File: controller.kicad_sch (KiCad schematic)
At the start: 3 parts

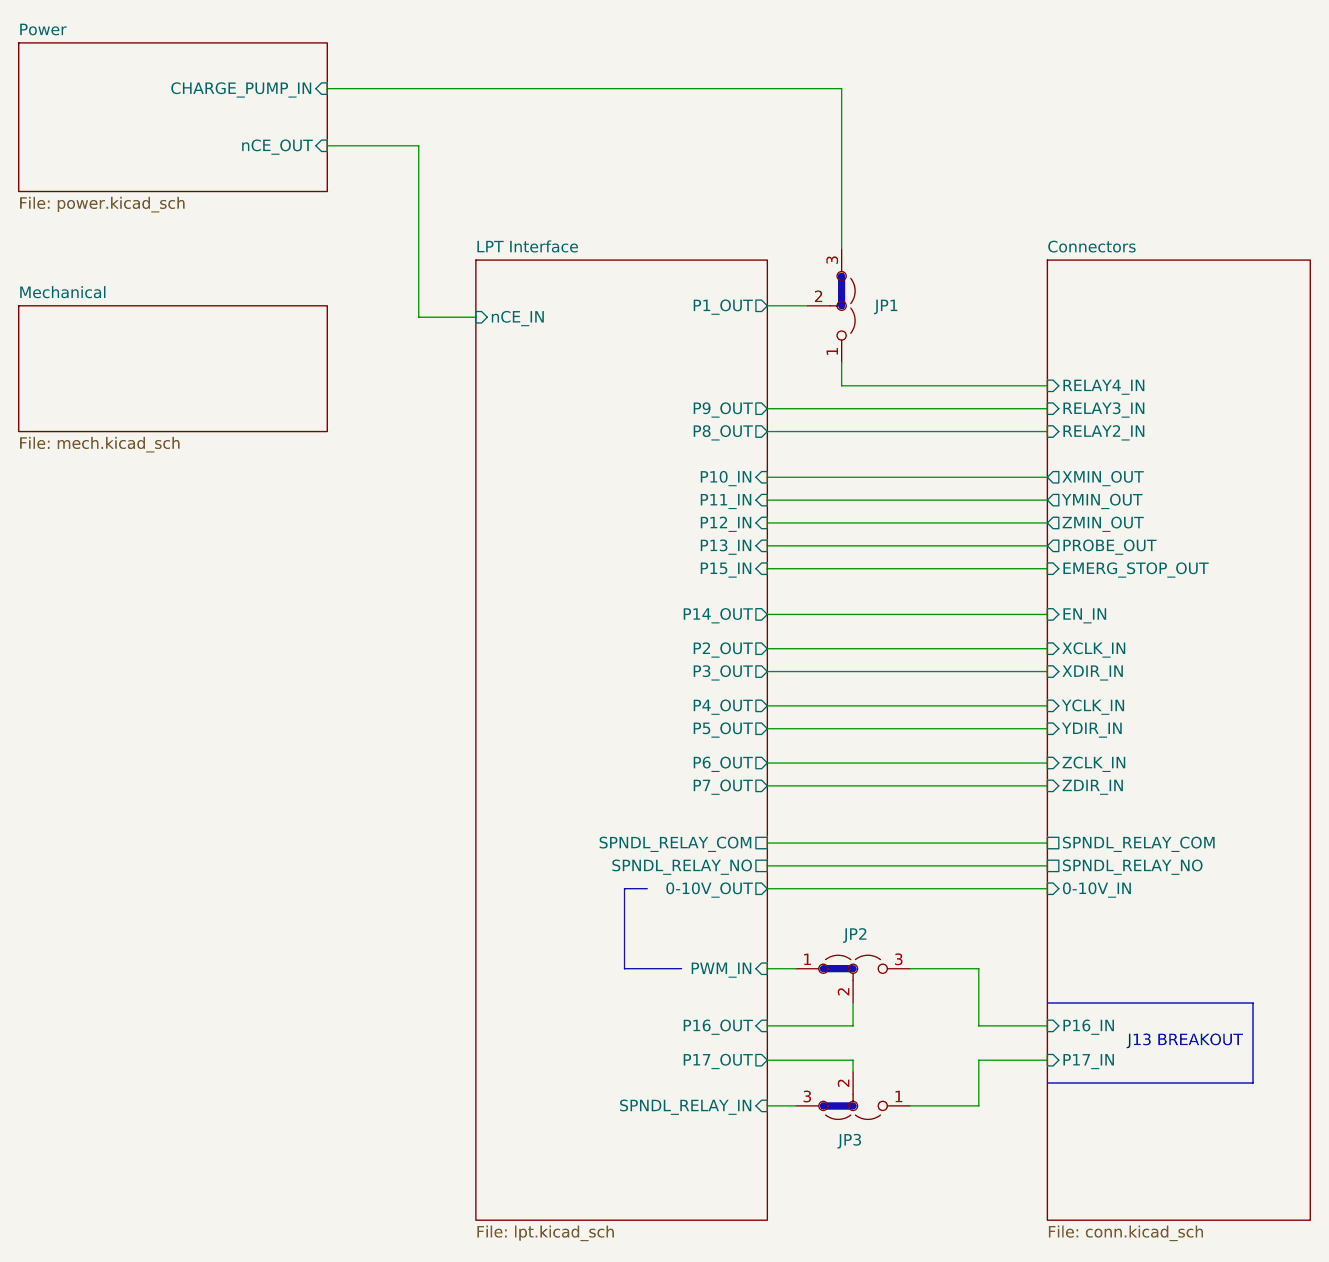
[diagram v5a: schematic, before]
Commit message: DRC checks. Tagging as V1.0 'actual'
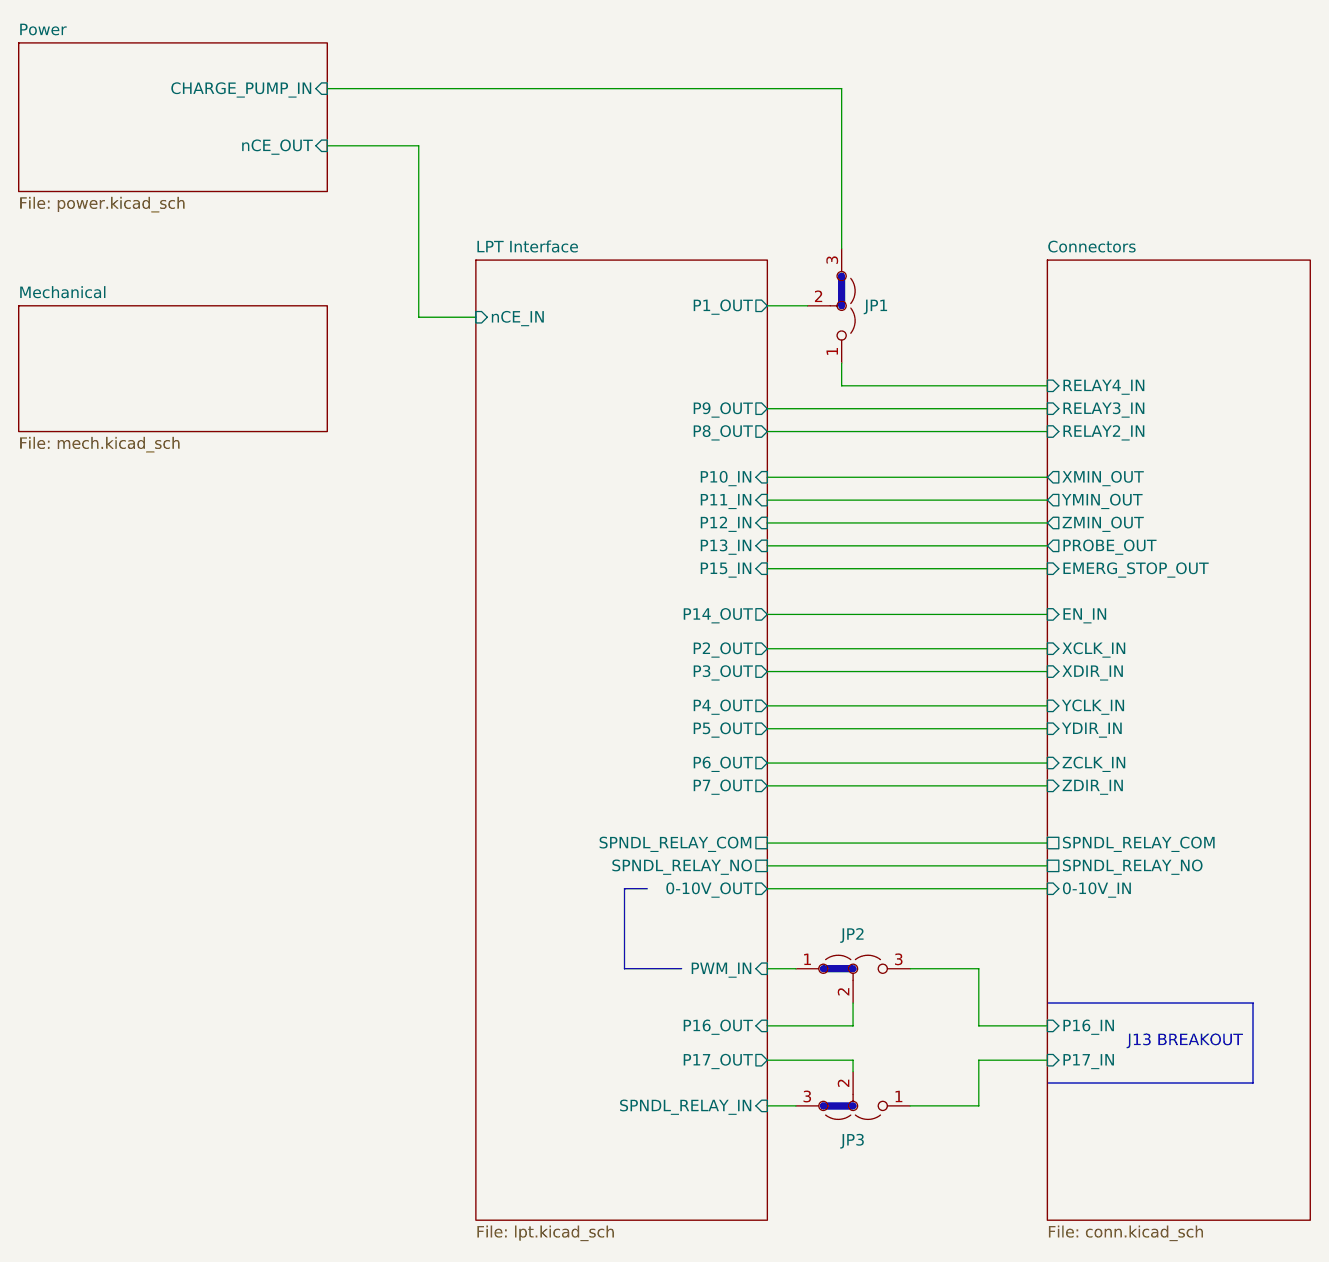
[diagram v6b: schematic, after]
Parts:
- JP1, JP2, JP3: value 1x02_2.54 -> (none); footprint Connector_PinHeader_2.54mm:PinHeader_1x03_P2.54mm_Vertical -> (none); E14MOQ 50 -> (none); E14PART 1593411 -> (none); JLCMFR# DNI -> (none)
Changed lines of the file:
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@@
+    (stroke (width 0) (type default) (color 0 0 0 0))
+  )
+  (wire (pts (xy 154.305 120.65) (xy 185.42 120.65))
+    (stroke (width 0) (type default) (color 0 0 0 0))
+  )
+  (wire (pts (xy 177.8 147.32) (xy 177.8 142.24))
+    (stroke (width 0) (type default) (color 0 0 0 0))
+  )
+  (polyline (pts (xy 185.42 144.78) (xy 208.28 144.78))
+    (stroke (width 0) (type default) (color 0 0 0 0))
+  )
+  (wire (pts (xy 115.57 59.69) (xy 121.92 59.69))
+    (stroke (width 0) (type default) (color 0 0 0 0))
+  )
+  (wire (pts (xy 154.305 77.47) (xy 185.42 77.47))
+    (stroke (width 0) (type default) (color 0 0 0 0))
+  )
+  (wire (pts (xy 177.8 132.08) (xy 177.8 138.43))
+    (stroke (width 0) (type default) (color 0 0 0 0))
+  )
+  (wire (pts (xy 154.305 132.08) (xy 157.48 132.08))
+    (stroke (width 0) (type default) (color 0 0 0 0))
+  )
+  (wire (pts (xy 162.56 34.29) (xy 105.41 34.29))
+    (stroke (width 0) (type default) (color 0 0 0 0))
+  )
+  (wire (pts (xy 154.305 80.01) (xy 185.42 80.01))
+    (stroke (width 0) (type default) (color 0 0 0 0))
+  )
+  (wire (pts (xy 154.305 58.42) (xy 158.75 58.42))
+    (stroke (width 0) (type default) (color 0 0 0 0))
+  )
+  (polyline (pts (xy 138.43 132.08) (xy 138.43 123.19))
     (stroke (width 0) (type default) (color 0 0 0 0))
   )
   (wire (pts (xy 163.83 142.24) (xy 163.83 143.51))
-    (stroke (width 0) (type default) (color 0 0 0 0))
-  )
-  (wire (pts (xy 154.305 120.65) (xy 185.42 120.65))
-    (stroke (width 0) (type default) (color 0 0 0 0))
-  )
-  (wire (pts (xy 177.8 147.32) (xy 177.8 142.24))
-    (stroke (width 0) (type default) (color 0 0 0 0))
-  )
-  (polyline (pts (xy 185.42 144.78) (xy 208.28 144.78))
-    (stroke (width 0) (type default) (color 0 0 0 0))
-  )
-  (wire (pts (xy 115.57 59.69) (xy 121.92 59.69))
-    (stroke (width 0) (type default) (color 0 0 0 0))
-  )
-  (wire (pts (xy 154.305 77.47) (xy 185.42 77.47))
-    (stroke (width 0) (type default) (color 0 0 0 0))
-  )
-  (wire (pts (xy 177.8 132.08) (xy 177.8 138.43))
-    (stroke (width 0) (type default) (color 0 0 0 0))
-  )
-  (wire (pts (xy 154.305 132.08) (xy 157.48 132.08))
-    (stroke (width 0) (type default) (color 0 0 0 0))
-  )
-  (wire (pts (xy 162.56 34.29) (xy 105.41 34.29))
-    (stroke (width 0) (type default) (color 0 0 0 0))
-  )
-  (wire (pts (xy 154.305 80.01) (xy 185.42 80.01))
-    (stroke (width 0) (type default) (color 0 0 0 0))
-  )
-  (wire (pts (xy 154.305 58.42) (xy 158.75 58.42))
-    (stroke (width 0) (type default) (color 0 0 0 0))
-  )
-  (polyline (pts (xy 138.43 132.08) (xy 138.43 123.19))
     (stroke (width 0) (type default) (color 0 0 0 0))
   )
@@
   )
   (symbol (lib_id "Jumper:Jumper_3_Open") (at 162.56 58.42 270) (mirror x) (unit 1)
-    (in_bom yes) (on_board yes)
-    (property "Reference" "JP1" (id 0) (at 168.91 58.42 90)
-      (effects (font (size 1.27 1.27)) (justify right))
-    )
-    (property "Value" "1x02_2.54" (id 1) (at 165.735 54.61 0)
-      (effects (font (size 1.27 1.27)) (justify right) hide)
-    )
-    (property "Footprint" "Connector_PinHeader_2.54mm:PinHeader_1x03_P2.54mm_Vertical" (id 2) (at 162.56 58.42 0)
+    (in_bom yes) (on_board yes) (fields_autoplaced)
+    (property "Reference" "JP1" (id 0) (at 165.1 58.4199 90)
+      (effects (font (size 1.27 1.27)) (justify left))
+    )
+    (property "Value" "" (id 1) (at 165.1 59.6899 90)
+      (effects (font (size 1.27 1.27)) (justify left) hide)
+    )
+    (property "Footprint" "" (id 2) (at 162.56 58.42 0)
       (effects (font (size 1.27 1.27)) hide)
     )
     (property "Datasheet" "~" (id 3) (at 162.56 58.42 0)
-      (effects (font (size 1.27 1.27)) hide)
-    )
-    (property "E14MOQ" "50" (id 5) (at 162.56 58.42 0)
-      (effects (font (size 1.27 1.27)) hide)
-    )
-    (property "E14PART" "1593411" (id 6) (at 162.56 58.42 0)
-      (effects (font (size 1.27 1.27)) hide)
-    )
-    (property "JLCMFR#" "DNI" (id 7) (at 162.56 58.42 0)
       (effects (font (size 1.27 1.27)) hide)
     )
@@
   )
   (symbol (lib_id "Jumper:Jumper_3_Open") (at 163.83 132.08 0) (unit 1)
-    (in_bom yes) (on_board yes)
-    (property "Reference" "JP2" (id 0) (at 165.481 128.27 0)
-      (effects (font (size 1.27 1.27)) (justify right))
-    )
-    (property "Value" "1x02_2.54" (id 1) (at 167.64 128.905 0)
-      (effects (font (size 1.27 1.27)) (justify right) hide)
-    )
-    (property "Footprint" "Connector_PinHeader_2.54mm:PinHeader_1x03_P2.54mm_Vertical" (id 2) (at 163.83 132.08 0)
+    (in_bom yes) (on_board yes) (fields_autoplaced)
+    (property "Reference" "JP2" (id 0) (at 163.83 128.27 0))
+    (property "Value" "" (id 1) (at 162.5601 129.54 90)
+      (effects (font (size 1.27 1.27)) (justify left) hide)
+    )
+    (property "Footprint" "" (id 2) (at 163.83 132.08 0)
       (effects (font (size 1.27 1.27)) hide)
     )
     (property "Datasheet" "~" (id 3) (at 163.83 132.08 0)
-      (effects (font (size 1.27 1.27)) hide)
-    )
-    (property "E14MOQ" "50" (id 5) (at 163.83 132.08 0)
-      (effects (font (size 1.27 1.27)) hide)
-    )
-    (property "E14PART" "1593411" (id 6) (at 163.83 132.08 0)
-      (effects (font (size 1.27 1.27)) hide)
-    )
-    (property "JLCMFR#" "DNI" (id 7) (at 163.83 132.08 0)
       (effects (font (size 1.27 1.27)) hide)
     )
@@
   )
   (symbol (lib_id "Jumper:Jumper_3_Open") (at 163.83 147.32 180) (unit 1)
-    (in_bom yes) (on_board yes)
-    (property "Reference" "JP3" (id 0) (at 162.179 151.13 0)
-      (effects (font (size 1.27 1.27)) (justify right))
-    )
-    (property "Value" "1x02_2.54" (id 1) (at 160.02 150.495 0)
-      (effects (font (size 1.27 1.27)) (justify right) hide)
-    )
-    (property "Footprint" "Connector_PinHeader_2.54mm:PinHeader_1x03_P2.54mm_Vertical" (id 2) (at 163.83 147.32 0)
+    (in_bom yes) (on_board yes) (fields_autoplaced)
+    (property "Reference" "JP3" (id 0) (at 163.83 151.13 0))
+    (property "Value" "" (id 1) (at 165.0999 149.86 90)
+      (effects (font (size 1.27 1.27)) (justify left) hide)
+    )
+    (property "Footprint" "" (id 2) (at 163.83 147.32 0)
       (effects (font (size 1.27 1.27)) hide)
     )
     (property "Datasheet" "~" (id 3) (at 163.83 147.32 0)
-      (effects (font (size 1.27 1.27)) hide)
-    )
-    (property "E14MOQ" "50" (id 5) (at 163.83 147.32 0)
-      (effects (font (size 1.27 1.27)) hide)
-    )
-    (property "E14PART" "1593411" (id 6) (at 163.83 147.32 0)
-      (effects (font (size 1.27 1.27)) hide)
-    )
-    (property "JLCMFR#" "DNI" (id 7) (at 163.83 147.32 0)
       (effects (font (size 1.27 1.27)) hide)
     )
@@
       (reference "#FLG03") (unit 1) (value "PWR_FLAG") (footprint "")
     )
+    (path "/91071e44-e7cf-47b2-b33b-9fbb68533ee5/aed2ffdd-38f1-4fa4-afad-7636c596bc94"
+      (reference "#FLG04") (unit 1) (value "PWR_FLAG") (footprint "")
+    )
     (path "/91071e44-e7cf-47b2-b33b-9fbb68533ee5/a975519f-ed25-4aa3-9b1c-75e817a3cc0e"
-      (reference "#FLG04") (unit 1) (value "PWR_FLAG") (footprint "")
+      (reference "#FLG05") (unit 1) (value "PWR_FLAG") (footprint "")
     )
     (path "/954a9830-ad6d-4d7c-92ee-21f7ecb42ef4/246b6006-16a2-4063-96ac-3d1f07d6eff1"
-      (reference "#FLG05") (unit 1) (value "PWR_FLAG") (footprint "")
+      (reference "#FLG06") (unit 1) (value "PWR_FLAG") (footprint "")
     )
     (path "/91071e44-e7cf-47b2-b33b-9fbb68533ee5/9625d2cc-68a9-4f1e-bbd5-e5d725d1c9c4"
@@
       (reference "J17") (unit 1) (value "MLX_1x03") (footprint "Connector_Molex:Molex_KK-254_AE-6410-03A_1x03_P2.54mm_Vertical")
     )
-    (path "/222d8c0b-93ab-4f32-bfba-fa69a8149f94"
-      (reference "JP1") (unit 1) (value "1x02_2.54") (footprint "Connector_PinHeader_2.54mm:PinHeader_1x03_P2.54mm_Vertical")
-    )
-    (path "/cc1f2c12-9849-40ea-87ab-71da88583597"
-      (reference "JP2") (unit 1) (value "1x02_2.54") (footprint "Connector_PinHeader_2.54mm:PinHeader_1x03_P2.54mm_Vertical")
-    )
-    (path "/e99af438-75fd-4a40-9a1c-0123ab9d9487"
-      (reference "JP3") (unit 1) (value "1x02_2.54") (footprint "Connector_PinHeader_2.54mm:PinHeader_1x03_P2.54mm_Vertical")
+    (path "/2e9e13a9-e196-4b72-bc93-fe719da0814a"
+      (reference "JP1") (unit 1) (value "1x03_2.54") (footprint "Connector_PinHeader_2.54mm:PinHeader_1x03_P2.54mm_Vertical")
+    )
+    (path "/6b063d77-942b-49dd-8948-b92dc588149d"
+      (reference "JP2") (unit 1) (value "1x03_2.54") (footprint "Connector_PinHeader_2.54mm:PinHeader_1x03_P2.54mm_Vertical")
+    )
+    (path "/b1f18de7-3994-4902-837a-833197abb796"
+      (reference "JP3") (unit 1) (value "1x03_2.54") (footprint "Connector_PinHeader_2.54mm:PinHeader_1x03_P2.54mm_Vertical")
     )
     (path "/91071e44-e7cf-47b2-b33b-9fbb68533ee5/490b02c5-0e78-4f5d-b25e-13628ef2b9fe"

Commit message: Lost the top layer ground plane. Got sick of being in Via Hell.
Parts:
- JP1, JP2, JP3: value (none) -> 1x03_2.54; footprint (none) -> Connector_PinHeader_2.54mm:PinHeader_1x03_P2.54mm_Vertical
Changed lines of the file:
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@@
       (effects (font (size 1.27 1.27)) (justify left))
     )
-    (property "Value" "" (id 1) (at 165.1 59.6899 90)
+    (property "Value" "1x03_2.54" (id 1) (at 165.1 59.6899 90)
       (effects (font (size 1.27 1.27)) (justify left) hide)
     )
-    (property "Footprint" "" (id 2) (at 162.56 58.42 0)
+    (property "Footprint" "Connector_PinHeader_2.54mm:PinHeader_1x03_P2.54mm_Vertical" (id 2) (at 162.56 58.42 0)
       (effects (font (size 1.27 1.27)) hide)
     )
@@
     (in_bom yes) (on_board yes) (fields_autoplaced)
     (property "Reference" "JP2" (id 0) (at 163.83 128.27 0))
-    (property "Value" "" (id 1) (at 162.5601 129.54 90)
+    (property "Value" "1x03_2.54" (id 1) (at 162.5601 129.54 90)
       (effects (font (size 1.27 1.27)) (justify left) hide)
     )
-    (property "Footprint" "" (id 2) (at 163.83 132.08 0)
+    (property "Footprint" "Connector_PinHeader_2.54mm:PinHeader_1x03_P2.54mm_Vertical" (id 2) (at 163.83 132.08 0)
       (effects (font (size 1.27 1.27)) hide)
     )
@@
     (in_bom yes) (on_board yes) (fields_autoplaced)
     (property "Reference" "JP3" (id 0) (at 163.83 151.13 0))
-    (property "Value" "" (id 1) (at 165.0999 149.86 90)
+    (property "Value" "1x03_2.54" (id 1) (at 165.0999 149.86 90)
       (effects (font (size 1.27 1.27)) (justify left) hide)
     )
-    (property "Footprint" "" (id 2) (at 163.83 147.32 0)
+    (property "Footprint" "Connector_PinHeader_2.54mm:PinHeader_1x03_P2.54mm_Vertical" (id 2) (at 163.83 147.32 0)
       (effects (font (size 1.27 1.27)) hide)
     )
